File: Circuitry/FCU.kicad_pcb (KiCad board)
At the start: 2 copper layers, 29 parts, among them J1 Conn_01x04_Pin, J2 USB_C_Receptacle_USB2.0_16P, J3 Conn_01x06_Pin, J4 Conn_01x04_Pin, J5 Conn_01x04_Pin, SW1 SW_SPDT, SW2 SW_Push, U1 STM32F405RGTx, U2 AMS1117-3.3, Y1 8MHz

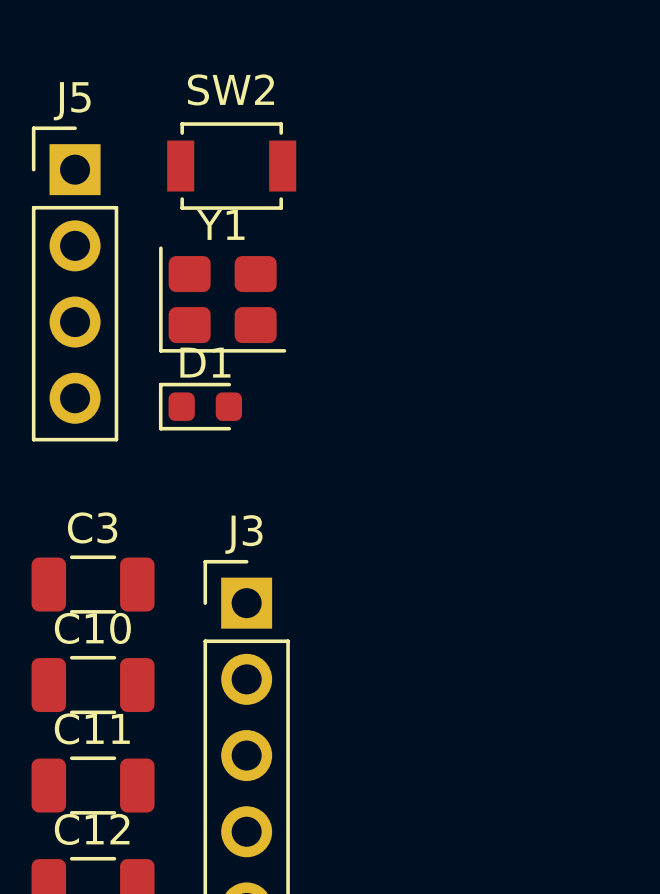
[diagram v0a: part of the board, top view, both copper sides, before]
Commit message: created FCU symbol and footprint libraries, add documentation, did some tests in STM32 project
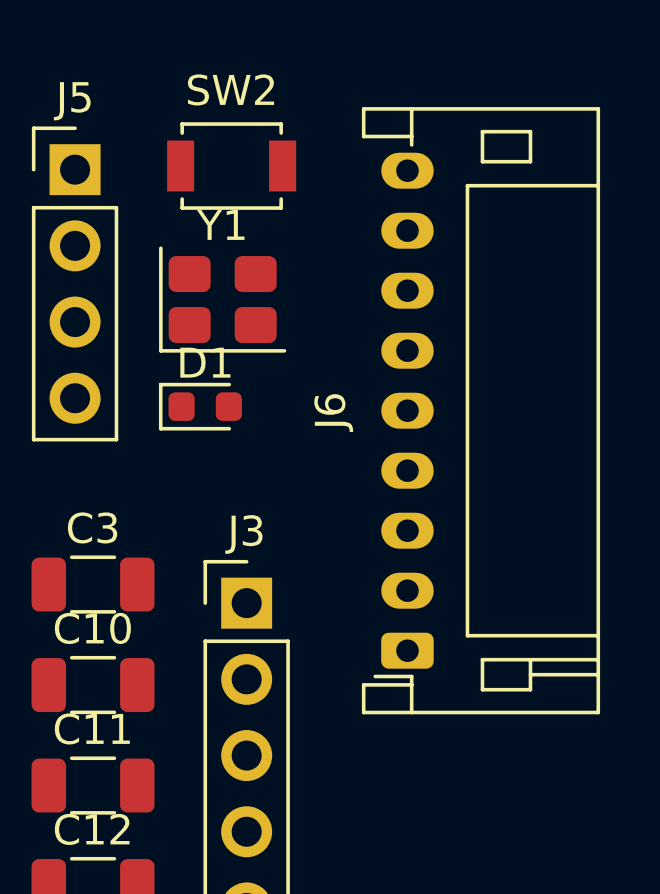
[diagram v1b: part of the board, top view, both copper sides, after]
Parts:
- added J6: Conn_01x09_Pin, Connector_JST:JST_PH_S9B-PH-K_1x09_P2.00mm_Horizontal, F.Cu at (88.5, 39.4)
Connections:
- U1 pad 39: unconnected-(U1-PC8-Pad39) -> SDIO_D0
- U1 pad 40: unconnected-(U1-PC9-Pad40) -> SDIO_D1
- U1 pad 50: unconnected-(U1-PA15-Pad50) -> SD_STS
- U1 pad 51: unconnected-(U1-PC10-Pad51) -> SDIO_D2
- U1 pad 52: unconnected-(U1-PC11-Pad52) -> SDIO_D3
- U1 pad 53: unconnected-(U1-PC12-Pad53) -> SDIO_CK
- U1 pad 54: unconnected-(U1-PD2-Pad54) -> SDIO_CMD
